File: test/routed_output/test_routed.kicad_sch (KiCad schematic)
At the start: 3 parts, among them U1 CP_Radial_D25.0mm_P10.00mm_Sn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, U2 R_Axial_DIN0207_L6.3mm_D2.5mm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, U3 R_Axial_DIN0207_L6.3mm_D2.5mm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

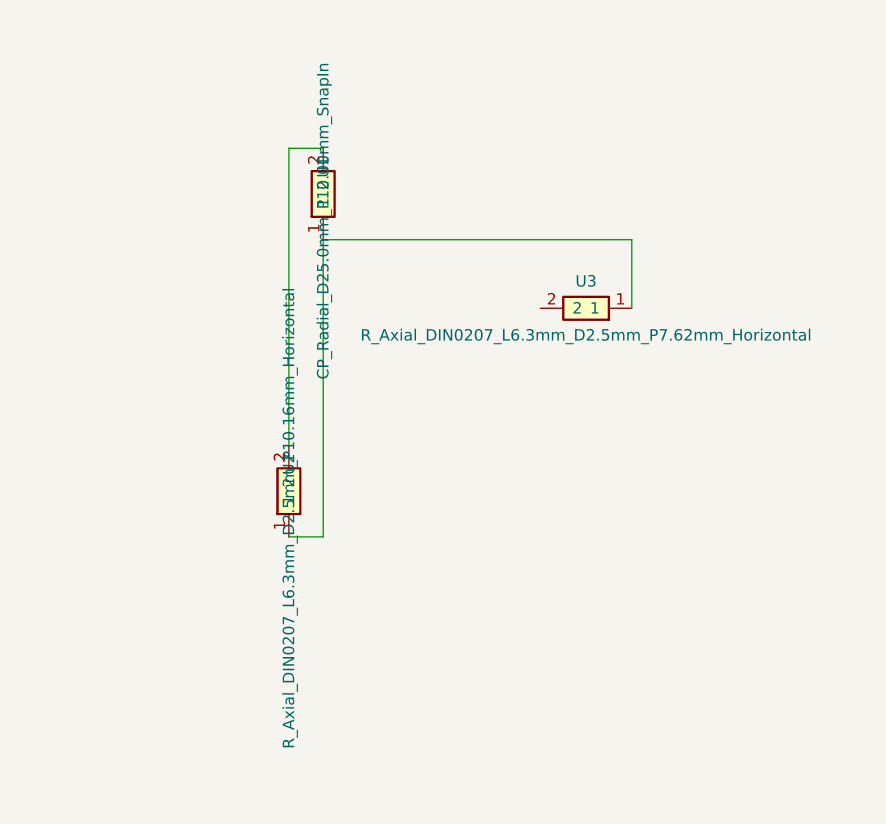
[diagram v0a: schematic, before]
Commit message: fix: schematic router - pin_map mapping + rotation formula alignment
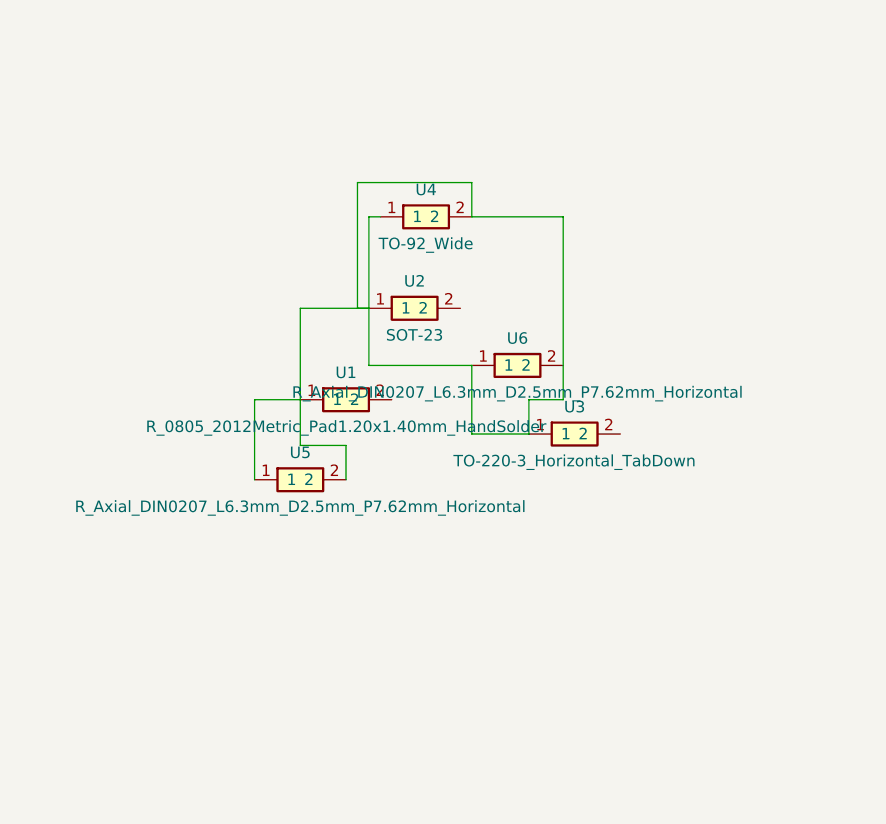
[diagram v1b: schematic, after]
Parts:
- removed U1: CP_Radial_D25.0mm_P10.00mm_SnapIn, 00_basic:CP_Radial_D25.0mm_P10.00mm_SnapIn, symbol 00_basic:C_Polarized
- removed U2: R_Axial_DIN0207_L6.3mm_D2.5mm_P10.16mm_Horizontal, 00_basic:R_Axial_DIN0207_L6.3mm_D2.5mm_P10.16mm_Horizontal, symbol 00_basic:R
- removed U3: R_Axial_DIN0207_L6.3mm_D2.5mm_P7.62mm_Horizontal, 00_basic:R_Axial_DIN0207_L6.3mm_D2.5mm_P7.62mm_Horizontal, symbol _placeholder:U3
- added U1: R_0805_2012Metric_Pad1.20x1.40mm_HandSolder, 00_basic:R_0805_2012Metric_Pad1.20x1.40mm_HandSolder, symbol RE_passive:R
- added U2: SOT-23, RE_active:SOT-23, symbol RE_active:Q_NPN
- added U3: TO-220-3_Horizontal_TabDown, RE_active:TO-220-3_Horizontal_TabDown, symbol RE_active:Q_NMOS
- added U4: TO-92_Wide, RE_active:TO-92_Wide, symbol RE_active:Q_NPN
- added U5: R_Axial_DIN0207_L6.3mm_D2.5mm_P7.62mm_Horizontal, RE_passive_tht:R_Axial_DIN0207_L6.3mm_D2.5mm_P7.62mm_Horizontal, symbol _placeholder:U5
- added U6: R_Axial_DIN0207_L6.3mm_D2.5mm_P7.62mm_Horizontal, RE_passive_tht:R_Axial_DIN0207_L6.3mm_D2.5mm_P7.62mm_Horizontal, symbol _placeholder:U6
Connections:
- new net: U1.1, U2.1, U3.1, U4.1, U4.2, U5.1, U5.2, U6.1
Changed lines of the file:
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@@
   (paper "A4")
   (symbol
-    (lib_id "00_basic:C_Polarized")
-    (at 135.89 88.90 90)
-    (unit 1)
-    (exclude_from_sim no)
-    (in_bom yes)
-    (on_board yes)
-    (dnp no)
-    (property "Reference" "U1" (at 135.89 85.90 0)
-      (effects (font (size 1.27 1.27)))
-    )
-    (property "Value" "CP_Radial_D25.0mm_P10.00mm_SnapIn" (at 135.89 91.90 0)
-      (effects (font (size 1.27 1.27)))
-    )
-    (property "Footprint" "00_basic:CP_Radial_D25.0mm_P10.00mm_SnapIn" (at 135.89 93.90 0)
+    (lib_id "RE_passive:R")
+    (at 138.43 111.76 0)
+    (unit 1)
+    (exclude_from_sim no)
+    (in_bom yes)
+    (on_board yes)
+    (dnp no)
+    (property "Reference" "U1" (at 138.43 108.76 0)
+      (effects (font (size 1.27 1.27)))
+    )
+    (property "Value" "R_0805_2012Metric_Pad1.20x1.40mm_HandSolder" (at 138.43 114.76 0)
+      (effects (font (size 1.27 1.27)))
+    )
+    (property "Footprint" "00_basic:R_0805_2012Metric_Pad1.20x1.40mm_HandSolder" (at 138.43 116.76 0)
       (effects (font (size 1.27 1.27)) hide)
     )
@@
   )
   (symbol
-    (lib_id "00_basic:R")
-    (at 132.08 121.92 90)
-    (unit 1)
-    (exclude_from_sim no)
-    (in_bom yes)
-    (on_board yes)
-    (dnp no)
-    (property "Reference" "U2" (at 132.08 118.92 0)
-      (effects (font (size 1.27 1.27)))
-    )
-    (property "Value" "R_Axial_DIN0207_L6.3mm_D2.5mm_P10.16mm_Horizontal" (at 132.08 124.92 0)
-      (effects (font (size 1.27 1.27)))
-    )
-    (property "Footprint" "00_basic:R_Axial_DIN0207_L6.3mm_D2.5mm_P10.16mm_Horizontal" (at 132.08 126.92 0)
+    (lib_id "RE_active:Q_NPN")
+    (at 146.05 101.60 0)
+    (unit 1)
+    (exclude_from_sim no)
+    (in_bom yes)
+    (on_board yes)
+    (dnp no)
+    (property "Reference" "U2" (at 146.05 98.60 0)
+      (effects (font (size 1.27 1.27)))
+    )
+    (property "Value" "SOT-23" (at 146.05 104.60 0)
+      (effects (font (size 1.27 1.27)))
+    )
+    (property "Footprint" "RE_active:SOT-23" (at 146.05 106.60 0)
       (effects (font (size 1.27 1.27)) hide)
     )
@@
   )
   (symbol
-    (lib_id "_placeholder:U3")
-    (at 165.10 101.60 180)
-    (unit 1)
-    (exclude_from_sim no)
-    (in_bom yes)
-    (on_board yes)
-    (dnp no)
-    (property "Reference" "U3" (at 165.10 98.60 0)
-      (effects (font (size 1.27 1.27)))
-    )
-    (property "Value" "R_Axial_DIN0207_L6.3mm_D2.5mm_P7.62mm_Horizontal" (at 165.10 104.60 0)
-      (effects (font (size 1.27 1.27)))
-    )
-    (property "Footprint" "00_basic:R_Axial_DIN0207_L6.3mm_D2.5mm_P7.62mm_Horizontal" (at 165.10 106.60 0)
+    (lib_id "RE_active:Q_NMOS")
+    (at 163.83 115.57 0)
+    (unit 1)
+    (exclude_from_sim no)
+    (in_bom yes)
+    (on_board yes)
+    (dnp no)
+    (property "Reference" "U3" (at 163.83 112.57 0)
+      (effects (font (size 1.27 1.27)))
+    )
+    (property "Value" "TO-220-3_Horizontal_TabDown" (at 163.83 118.57 0)
+      (effects (font (size 1.27 1.27)))
+    )
+    (property "Footprint" "RE_active:TO-220-3_Horizontal_TabDown" (at 163.83 120.57 0)
       (effects (font (size 1.27 1.27)) hide)
     )
@@
     )
   )
-  (wire (pts (xy 132.08 116.84) (xy 132.08 83.82))
-    (stroke (width 0) (type default))
-  )
-  (wire (pts (xy 132.08 83.82) (xy 135.89 83.82))
-    (stroke (width 0) (type default))
-  )
-  (wire (pts (xy 170.18 101.60) (xy 170.18 93.98))
-    (stroke (width 0) (type default))
-  )
-  (wire (pts (xy 170.18 93.98) (xy 135.89 93.98))
-    (stroke (width 0) (type default))
-  )
-  (wire (pts (xy 135.89 93.98) (xy 135.89 127.00))
-    (stroke (width 0) (type default))
-  )
-  (wire (pts (xy 135.89 127.00) (xy 132.08 127.00))
-    (stroke (width 0) (type default))
-  )
+  (symbol
+    (lib_id "RE_active:Q_NPN")
+    (at 147.32 91.44 0)
+    (unit 1)
+    (exclude_from_sim no)
+    (in_bom yes)
+    (on_board yes)
+    (dnp no)
+    (property "Reference" "U4" (at 147.32 88.44 0)
+      (effects (font (size 1.27 1.27)))
+    )
+    (property "Value" "TO-92_Wide" (at 147.32 94.44 0)
+      (effects (font (size 1.27 1.27)))
+    )
+    (property "Footprint" "RE_active:TO-92_Wide" (at 147.32 96.44 0)
+      (effects (font (size 1.27 1.27)) hide)
+    )
+    (instances
+      (project ""
+        (path "/"
+          (reference "U4")
+          (unit 1)
+        )
+      )
+    )
+  )
+  (symbol
+    (lib_id "_placeholder:U5")
+    (at 133.35 120.65 0)
+    (unit 1)
+    (exclude_from_sim no)
+    (in_bom yes)
+    (on_board yes)
+    (dnp no)
+    (property "Reference" "U5" (at 133.35 117.65 0)
+      (effects (font (size 1.27 1.27)))
+    )
+    (property "Value" "R_Axial_DIN0207_L6.3mm_D2.5mm_P7.62mm_Horizontal" (at 133.35 123.65 0)
+      (effects (font (size 1.27 1.27)))
+    )
+    (property "Footprint" "RE_passive_tht:R_Axial_DIN0207_L6.3mm_D2.5mm_P7.62mm_Horizontal" (at 133.35 125.65 0)
+      (effects (font (size 1.27 1.27)) hide)
+    )
+    (instances
+      (project ""
+        (path "/"
+          (reference "U5")
+          (unit 1)
+        )
+      )
+    )
+  )
+  (symbol
+    (lib_id "_placeholder:U6")
+    (at 157.48 107.95 0)
+    (unit 1)
+    (exclude_from_sim no)
+    (in_bom yes)
+    (on_board yes)
+    (dnp no)
+    (property "Reference" "U6" (at 157.48 104.95 0)
+      (effects (font (size 1.27 1.27)))
+    )
+    (property "Value" "R_Axial_DIN0207_L6.3mm_D2.5mm_P7.62mm_Horizontal" (at 157.48 110.95 0)
+      (effects (font (size 1.27 1.27)))
+    )
+    (property "Footprint" "RE_passive_tht:R_Axial_DIN0207_L6.3mm_D2.5mm_P7.62mm_Horizontal" (at 157.48 112.95 0)
+      (effects (font (size 1.27 1.27)) hide)
+    )
+    (instances
+      (project ""
+        (path "/"
+          (reference "U6")
+          (unit 1)
+        )
+      )
+    )
+  )
+  (wire (pts (xy 140.97 101.60) (xy 140.97 91.44))
+    (stroke (width 0) (type default))
+  )
+  (wire (pts (xy 140.97 91.44) (xy 142.24 91.44))
+    (stroke (width 0) (type default))
+  )
+  (wire (pts (xy 128.27 120.65) (xy 128.27 111.76))
+    (stroke (width 0) (type default))
+  )
+  (wire (pts (xy 128.27 111.76) (xy 133.35 111.76))
+    (stroke (width 0) (type default))
+  )
+  (wire (pts (xy 140.97 101.60) (xy 140.97 107.95))
+    (stroke (width 0) (type default))
+  )
+  (wire (pts (xy 140.97 107.95) (xy 152.40 107.95))
+    (stroke (width 0) (type default))
+  )
+  (wire (pts (xy 152.40 107.95) (xy 152.40 115.57))
+    (stroke (width 0) (type default))
+  )
+  (wire (pts (xy 152.40 115.57) (xy 158.75 115.57))
+    (stroke (width 0) (type default))
+  )
+  (wire (pts (xy 140.97 101.60) (xy 133.35 101.60))
+    (stroke (width 0) (type default))
+  )
+  (wire (pts (xy 133.35 101.60) (xy 133.35 111.76))
+    (stroke (width 0) (type default))
+  )
+  (wire (pts (xy 133.35 111.76) (xy 133.35 116.84))
+    (stroke (width 0) (type default))
+  )
+  (wire (pts (xy 133.35 116.84) (xy 138.43 116.84))
+    (stroke (width 0) (type default))
+  )
+  (wire (pts (xy 138.43 116.84) (xy 138.43 120.65))
+    (stroke (width 0) (type default))
+  )
+  (wire (pts (xy 140.97 101.60) (xy 139.70 101.60))
+    (stroke (width 0) (type default))
+  )
+  (wire (pts (xy 139.70 101.60) (xy 139.70 87.63))
+    (stroke (width 0) (type default))
+  )
+  (wire (pts (xy 139.70 87.63) (xy 152.40 87.63))
+    (stroke (width 0) (type default))
+  )
+  (wire (pts (xy 152.40 87.63) (xy 152.40 91.44))
+    (stroke (width 0) (type default))
+  )
+  (wire (pts (xy 152.40 91.44) (xy 162.56 91.44))
+    (stroke (width 0) (type default))
+  )
+  (wire (pts (xy 162.56 91.44) (xy 162.56 111.76))
+    (stroke (width 0) (type default))
+  )
+  (wire (pts (xy 162.56 111.76) (xy 158.75 111.76))
+    (stroke (width 0) (type default))
+  )
+  (wire (pts (xy 158.75 111.76) (xy 158.75 115.57))
+    (stroke (width 0) (type default))
+  )

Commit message: backup
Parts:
- added U7: CP_Radial_D30.0mm_P10.00mm_SnapIn, RE_passive_tht:CP_Radial_D30.0mm_P10.00mm_SnapIn, symbol RE_passive:C_Polarized
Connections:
- net at U1.1, U2.1, U3.1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: no longer U6.1
- net at U3.2: now also U7.2
